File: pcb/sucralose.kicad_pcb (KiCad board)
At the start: 2 copper layers, 141.8 x 89.9 mm, 70 parts, among them M1 MountingHole_1.2mm_M1

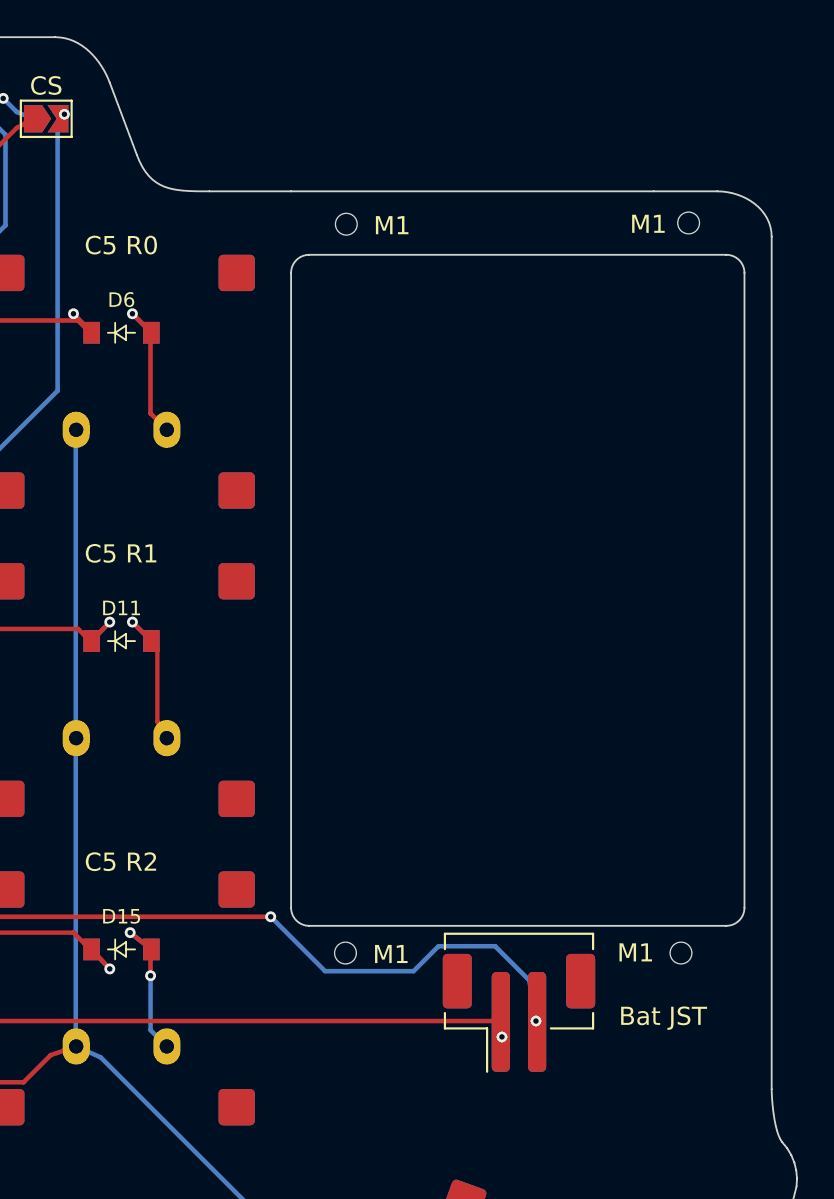
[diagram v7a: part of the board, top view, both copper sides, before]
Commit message: Lengthened the battery cutout area.
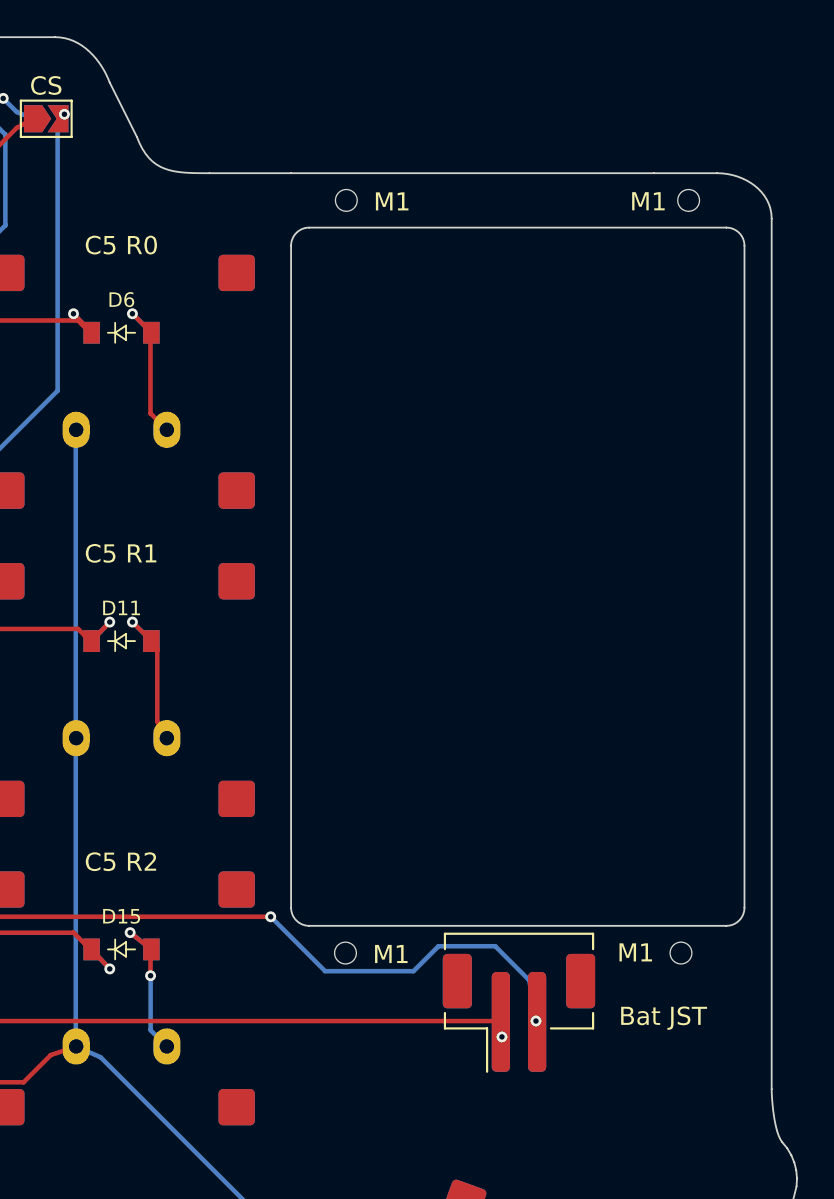
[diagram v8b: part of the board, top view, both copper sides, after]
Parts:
- moved M1 1.31 mm to (180.0, 58.0)
- moved M1 1.24 mm to (198.9, 58.0)
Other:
- outline, holes or cut-outs redrawn
